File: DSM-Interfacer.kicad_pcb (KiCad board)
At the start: 2 copper layers, 38.3 x 66.8 mm, 25 parts, among them J1 USB_B_Micro, J2 DIAG, Q1 BSS138, Q2 BSS138, Q3 MMBT2222A, SW1 RESET, SW2 BOOT/FLASH, U1 ESP32-WROOM-32, U2 MAX232, U3 CH340C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

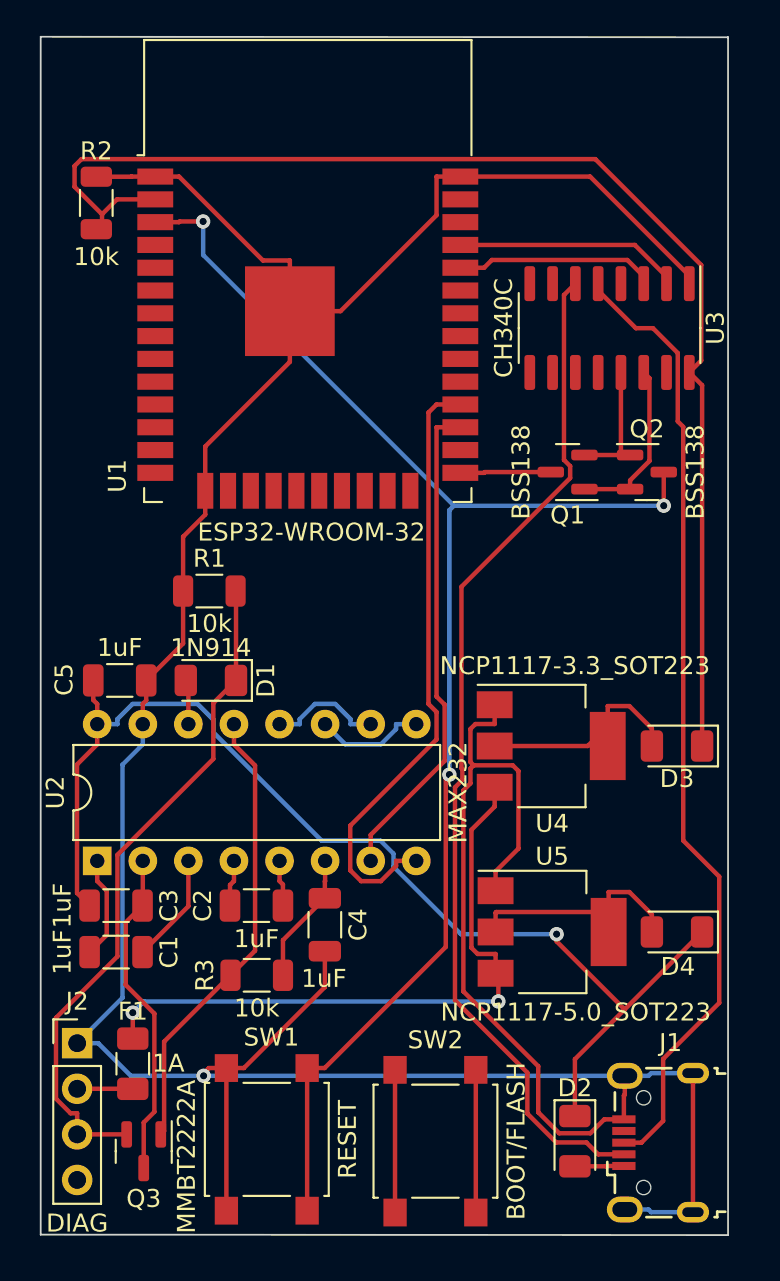
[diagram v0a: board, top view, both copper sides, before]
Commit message: smaller MAX323
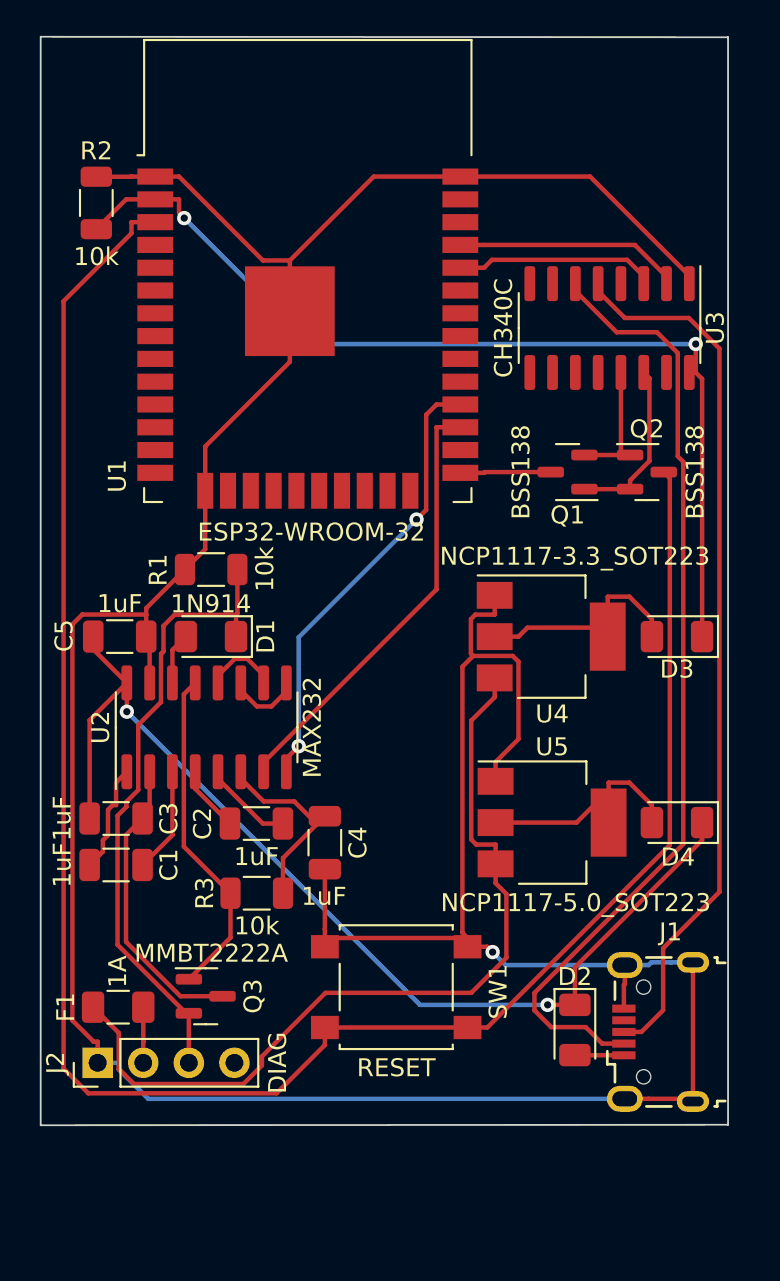
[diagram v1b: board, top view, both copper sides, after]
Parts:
- removed SW2: BOOT/FLASH, Button_Switch_SMD:SW_SPST_B3S-1000
- U2: footprint Package_DIP:DIP-16_W7.62mm -> Package_SO:SOIC-16_3.9x9.9mm_P1.27mm
- moved SW1 11.1 mm to (161.2, 115.9), turned to 0 degrees
- moved U2 9.62 mm to (150.7, 101.4)
- moved Q3 9.30 mm to (150.6, 116.4), turned to 0 degrees
- moved D2 6.20 mm to (171.2, 118.3)
- moved J1 6.17 mm to (175.8, 118.4)
- moved D3 6.10 mm to (176.9, 96.4)
- moved D4 6.10 mm to (176.9, 106.8)
- moved U4 6.10 mm to (169.9, 96.4)
- moved U5 6.10 mm to (169.9, 106.8)
- moved C1 4.85 mm to (145.6, 109.1)
- moved C3 4.85 mm to (145.6, 106.5)
- moved C2 4.57 mm to (153.5, 106.8)
- moved C4 4.57 mm to (157.3, 107.9)
- moved R3 4.57 mm to (153.5, 110.7)
- moved F1 3.25 mm to (145.7, 117.0), turned to 0 degrees
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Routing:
- net Net-(Q2-Pad3): track 81.1 -> 111.6 mm, vias 3 -> 0
- net +3V3: track 72.0 -> 54.7 mm, vias 0 -> 2
- net +12V: track 36.1 -> 46.8 mm, vias 2 -> 0
- net Net-(U1-Pad28): track 34.2 -> 25.3 mm, vias 0 -> 2
- net unconnected-(SW2-Pad2): track 7.95 -> 0.00 mm
- net unconnected-(SW2-Pad1): track 7.95 -> 0.00 mm
- net Net-(Q3-Pad1): track 25.5 -> 18.8 mm
- net +5V: track 64.7 -> 58.2 mm, vias 1 -> 2
- net Net-(J1-Pad3): track 53.6 -> 49.4 mm
- net Net-(J1-Pad2): track 57.3 -> 53.5 mm
- net Net-(C4-Pad1): track 7.35 -> 10.9 mm
- net Net-(U1-Pad27): track 27.4 -> 24.5 mm
- net /Data: track 37.9 -> 35.2 mm
- net Net-(C2-Pad2): track 2.57 -> 5.04 mm
- net Net-(U2-Pad10): track 6.34 -> 4.14 mm
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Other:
- board size 38.3 x 66.8 mm -> 38.3 x 60.7 mm
